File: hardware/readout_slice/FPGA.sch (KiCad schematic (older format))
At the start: 0 parts

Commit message: more work on moving FPGA components around
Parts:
- added U? (x5): XC7A35T-1FGG484, symbol readout:XC7A35T-1FGG484
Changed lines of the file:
@@
 $Descr A4 11693 8268
 encoding utf-8
-Sheet 1 4
+Sheet 4 4
 Title ""
 Date ""
@@
 Comment4 ""
 $EndDescr
+$Comp
+L readout:XC7A35T-1FGG484 U?
+U 4 1 6056B4FB
+P 1900 4550
+AR Path="/6056B4FB" Ref="U?"  Part="4"
+AR Path="/605605C8/6056B4FB" Ref="U?"  Part="4"
+F 0 "U?" H 1950 777 50  0000 C CNN
+F 1 "XC7A35T-1FGG484" H 1950 686 50  0000 C CNN
+F 2 "" H 800 4700 50  0001 C CNN
+F 3 "" H 800 4700 50  0001 C CNN
+	4    1900 4550
+	1    0    0    -1
+$EndComp
+$Comp
+L readout:XC7A35T-1FGG484 U?
+U 5 1 6056B501
+P 2150 -450
+AR Path="/6056B501" Ref="U?"  Part="5"
+AR Path="/605605C8/6056B501" Ref="U?"  Part="5"
+F 0 "U?" H 1825 -4223 50  0000 C CNN
+F 1 "XC7A35T-1FGG484" H 1825 -4314 50  0000 C CNN
+F 2 "" H 1050 -300 50  0001 C CNN
+F 3 "" H 1050 -300 50  0001 C CNN
+	5    2150 -450
+	1    0    0    -1
+$EndComp
+$Comp
+L readout:XC7A35T-1FGG484 U?
+U 6 1 6056B507
+P 5250 -50
+AR Path="/6056B507" Ref="U?"  Part="6"
+AR Path="/605605C8/6056B507" Ref="U?"  Part="6"
+F 0 "U?" H 5125 -3823 50  0000 C CNN
+F 1 "XC7A35T-1FGG484" H 5125 -3914 50  0000 C CNN
+F 2 "" H 4150 100 50  0001 C CNN
+F 3 "" H 4150 100 50  0001 C CNN
+	6    5250 -50
+	1    0    0    -1
+$EndComp
+$Comp
+L readout:XC7A35T-1FGG484 U?
+U 7 1 6057AABA
+P 8250 1800
+F 0 "U?" H 8125 -1973 50  0000 C CNN
+F 1 "XC7A35T-1FGG484" H 8125 -2064 50  0000 C CNN
+F 2 "" H 7150 1950 50  0001 C CNN
+F 3 "" H 7150 1950 50  0001 C CNN
+	7    8250 1800
+	1    0    0    -1
+$EndComp
+$Comp
+L readout:XC7A35T-1FGG484 U?
+U 8 1 6057AAC0
+P 11600 1550
+F 0 "U?" H 11225 -2223 50  0000 C CNN
+F 1 "XC7A35T-1FGG484" H 11225 -2314 50  0000 C CNN
+F 2 "" H 10500 1700 50  0001 C CNN
+F 3 "" H 10500 1700 50  0001 C CNN
+	8    11600 1550
+	1    0    0    -1
+$EndComp
 $EndSCHEMATC

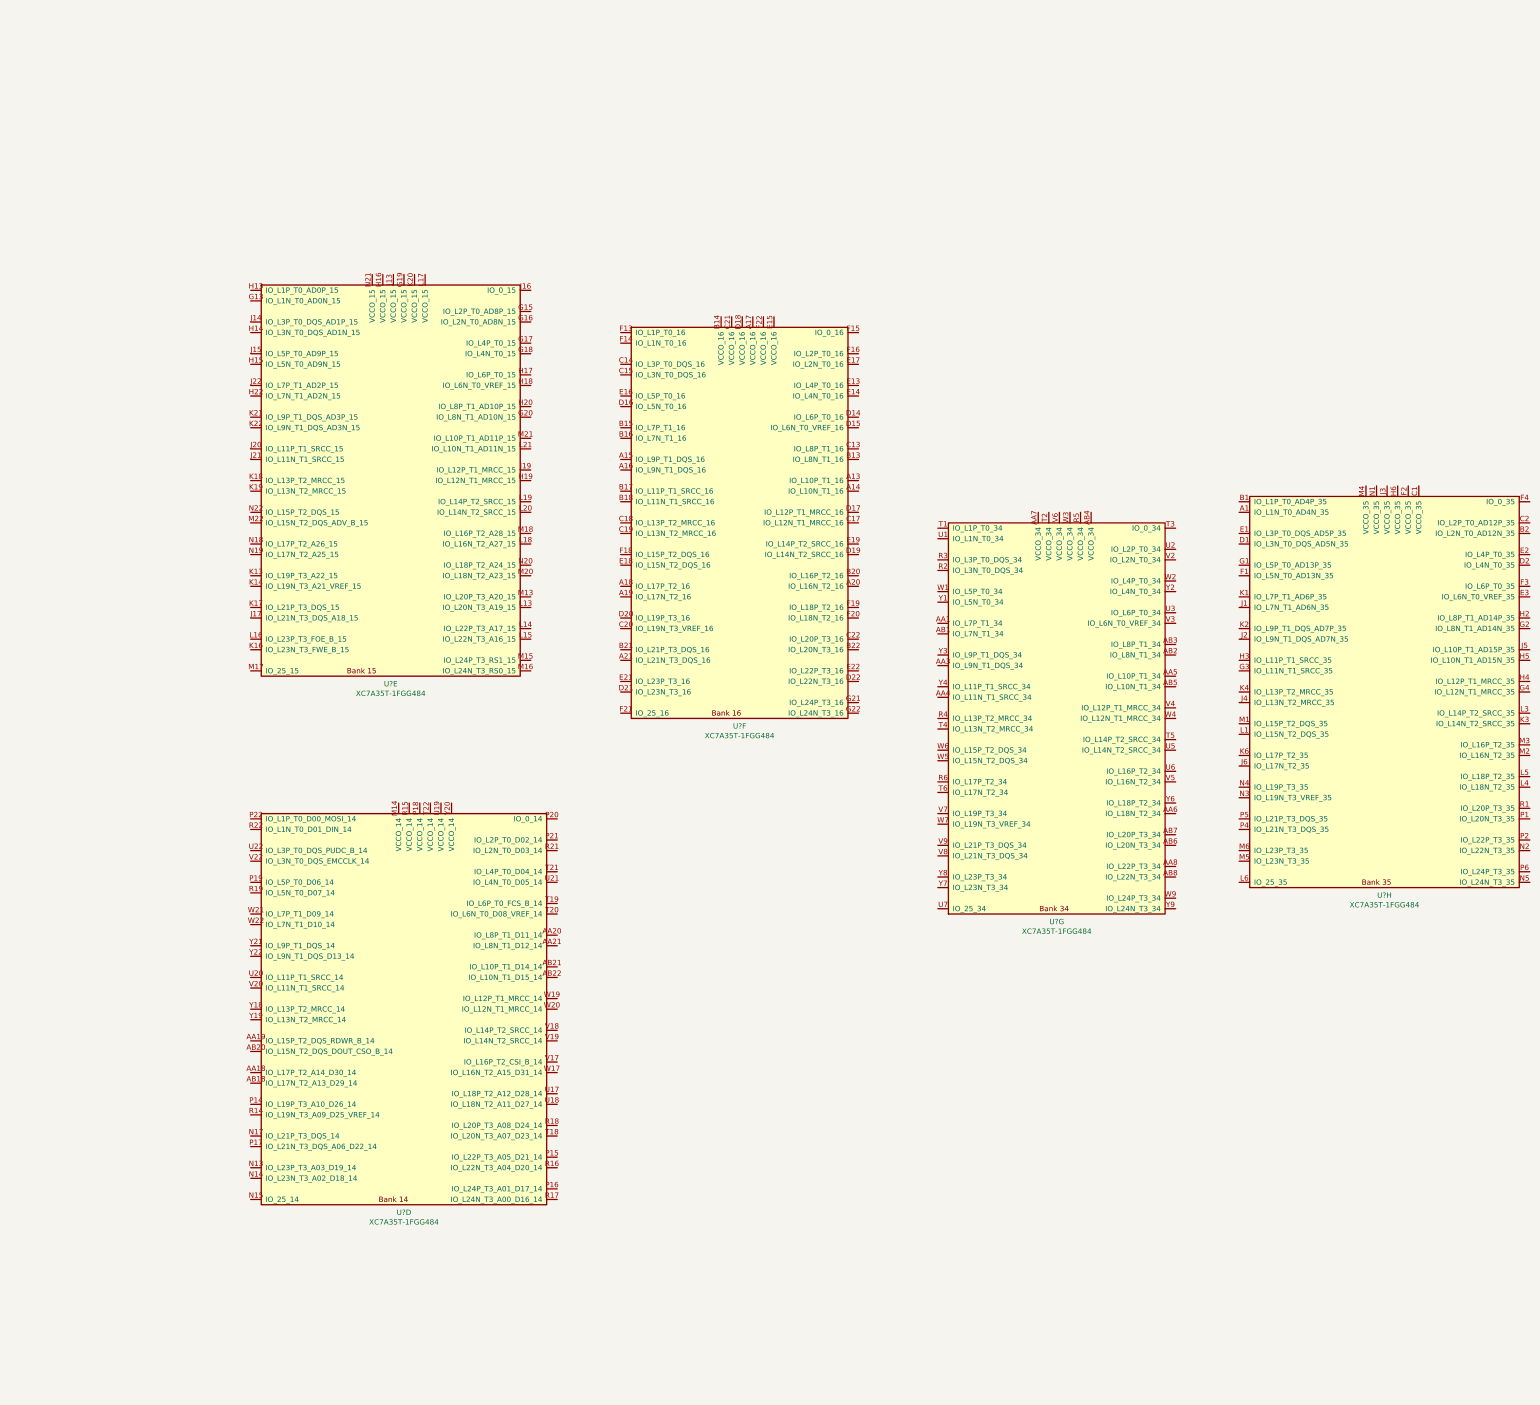
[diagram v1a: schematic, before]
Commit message: more work on readout connectivity
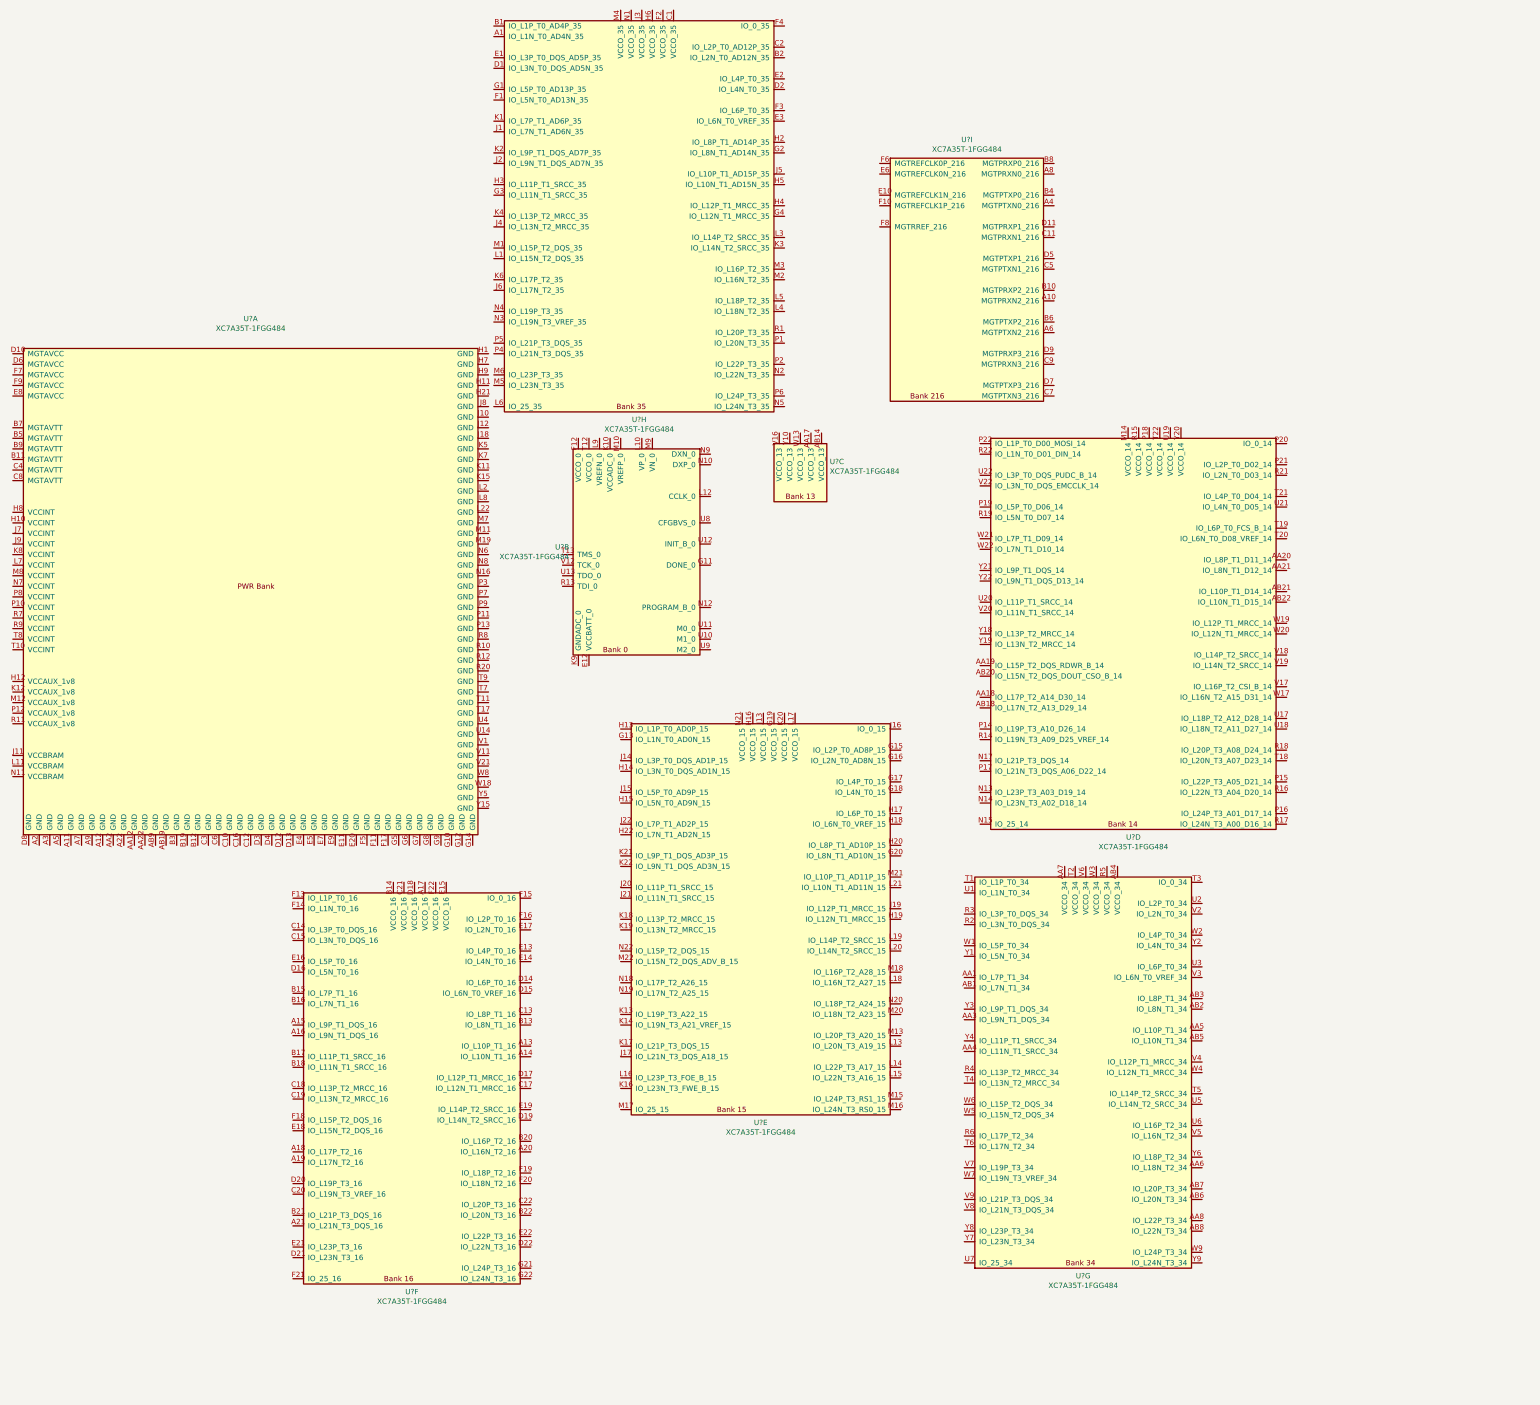
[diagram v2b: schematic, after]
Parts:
- removed U? (x5): XC7A35T-1FGG484, symbol readout:XC7A35T-1FGG484
- added U? (x9): XC7A35T-1FGG484, symbol readout:XC7A35T-1FGG484
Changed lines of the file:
@@
 $Comp
 L readout:XC7A35T-1FGG484 U?
-U 4 1 6056B4FB
-P 1900 4550
-AR Path="/6056B4FB" Ref="U?"  Part="4"
-AR Path="/605605C8/6056B4FB" Ref="U?"  Part="4"
-F 0 "U?" H 1950 777 50  0000 C CNN
-F 1 "XC7A35T-1FGG484" H 1950 686 50  0000 C CNN
-F 2 "" H 800 4700 50  0001 C CNN
-F 3 "" H 800 4700 50  0001 C CNN
-	4    1900 4550
+U 1 1 604A9F40
+P 650 150
+F 0 "U?" H 500 431 50  0000 C CNN
+F 1 "XC7A35T-1FGG484" H 500 340 50  0000 C CNN
+F 2 "" H -450 300 50  0001 C CNN
+F 3 "" H -450 300 50  0001 C CNN
+	1    650  150
 	1    0    0    -1
 $EndComp
 $Comp
 L readout:XC7A35T-1FGG484 U?
-U 5 1 6056B501
-P 2150 -450
-AR Path="/6056B501" Ref="U?"  Part="5"
-AR Path="/605605C8/6056B501" Ref="U?"  Part="5"
-F 0 "U?" H 1825 -4223 50  0000 C CNN
-F 1 "XC7A35T-1FGG484" H 1825 -4314 50  0000 C CNN
-F 2 "" H 1050 -300 50  0001 C CNN
-F 3 "" H 1050 -300 50  0001 C CNN
-	5    2150 -450
+U 2 1 604B4183
+P 4350 1100
+F 0 "U?" H 3513 171 50  0000 R CNN
+F 1 "XC7A35T-1FGG484" H 3513 80  50  0000 R CNN
+F 2 "" H 3250 1250 50  0001 C CNN
+F 3 "" H 3250 1250 50  0001 C CNN
+	2    4350 1100
 	1    0    0    -1
 $EndComp
 $Comp
 L readout:XC7A35T-1FGG484 U?
-U 6 1 6056B507
-P 5250 -50
-AR Path="/6056B507" Ref="U?"  Part="6"
-AR Path="/605605C8/6056B507" Ref="U?"  Part="6"
-F 0 "U?" H 5125 -3823 50  0000 C CNN
-F 1 "XC7A35T-1FGG484" H 5125 -3914 50  0000 C CNN
-F 2 "" H 4150 100 50  0001 C CNN
-F 3 "" H 4150 100 50  0001 C CNN
-	6    5250 -50
+U 3 1 604BC08F
+P 5700 1050
+F 0 "U?" H 5978 879 50  0000 L CNN
+F 1 "XC7A35T-1FGG484" H 5978 788 50  0000 L CNN
+F 2 "" H 4600 1200 50  0001 C CNN
+F 3 "" H 4600 1200 50  0001 C CNN
+	3    5700 1050
 	1    0    0    -1
 $EndComp
 $Comp
 L readout:XC7A35T-1FGG484 U?
-U 7 1 6057AABA
-P 8250 1800
-F 0 "U?" H 8125 -1973 50  0000 C CNN
-F 1 "XC7A35T-1FGG484" H 8125 -2064 50  0000 C CNN
-F 2 "" H 7150 1950 50  0001 C CNN
-F 3 "" H 7150 1950 50  0001 C CNN
-	7    8250 1800
+U 4 1 604C5353
+P 8800 1000
+F 0 "U?" H 8850 -2773 50  0000 C CNN
+F 1 "XC7A35T-1FGG484" H 8850 -2864 50  0000 C CNN
+F 2 "" H 7700 1150 50  0001 C CNN
+F 3 "" H 7700 1150 50  0001 C CNN
+	4    8800 1000
 	1    0    0    -1
 $EndComp
 $Comp
 L readout:XC7A35T-1FGG484 U?
-U 8 1 6057AAC0
-P 11600 1550
-F 0 "U?" H 11225 -2223 50  0000 C CNN
-F 1 "XC7A35T-1FGG484" H 11225 -2314 50  0000 C CNN
-F 2 "" H 10500 1700 50  0001 C CNN
-F 3 "" H 10500 1700 50  0001 C CNN
-	8    11600 1550
+U 5 1 604CE9F8
+P 5650 3700
+F 0 "U?" H 5325 -73 50  0000 C CNN
+F 1 "XC7A35T-1FGG484" H 5325 -164 50  0000 C CNN
+F 2 "" H 4550 3850 50  0001 C CNN
+F 3 "" H 4550 3850 50  0001 C CNN
+	5    5650 3700
 	1    0    0    -1
 $EndComp
+$Comp
+L readout:XC7A35T-1FGG484 U?
+U 6 1 604D9845
+P 2150 5300
+F 0 "U?" H 2025 1527 50  0000 C CNN
+F 1 "XC7A35T-1FGG484" H 2025 1436 50  0000 C CNN
+F 2 "" H 1050 5450 50  0001 C CNN
+F 3 "" H 1050 5450 50  0001 C CNN
+	6    2150 5300
+	1    0    0    -1
+$EndComp
+$Comp
+L readout:XC7A35T-1FGG484 U?
+U 7 1 604E2EDB
+P 8500 5150
+F 0 "U?" H 8375 1377 50  0000 C CNN
+F 1 "XC7A35T-1FGG484" H 8375 1286 50  0000 C CNN
+F 2 "" H 7400 5300 50  0001 C CNN
+F 3 "" H 7400 5300 50  0001 C CNN
+	7    8500 5150
+	1    0    0    -1
+$EndComp
+$Comp
+L readout:XC7A35T-1FGG484 U?
+U 8 1 604EB97A
+P 4550 -2950
+F 0 "U?" H 4175 -6723 50  0000 C CNN
+F 1 "XC7A35T-1FGG484" H 4175 -6814 50  0000 C CNN
+F 2 "" H 3450 -2800 50  0001 C CNN
+F 3 "" H 3450 -2800 50  0001 C CNN
+	8    4550 -2950
+	1    0    0    -1
+$EndComp
+$Comp
+L readout:XC7A35T-1FGG484 U?
+U 9 1 6050DA52
+P 7350 -1650
+F 0 "U?" H 7275 -1475 50  0000 C CNN
+F 1 "XC7A35T-1FGG484" H 7275 -1566 50  0000 C CNN
+F 2 "" H 6250 -1500 50  0001 C CNN
+F 3 "" H 6250 -1500 50  0001 C CNN
+	9    7350 -1650
+	1    0    0    -1
+$EndComp

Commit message: more work on readout_slice
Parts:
- removed U?: XC7A35T-1FGG484, symbol readout:XC7A35T-1FGG484
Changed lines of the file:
@@
-$Comp
-L readout:XC7A35T-1FGG484 U?
-U 1 1 604A9F40
-P 650 150
-F 0 "U?" H 500 431 50  0000 C CNN
-F 1 "XC7A35T-1FGG484" H 500 340 50  0000 C CNN
-F 2 "" H -450 300 50  0001 C CNN
-F 3 "" H -450 300 50  0001 C CNN
-	1    650  150
-	1    0    0    -1
-$EndComp
 $Comp
 L readout:XC7A35T-1FGG484 U?

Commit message: working more on readout_slice schematic
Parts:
- removed U?: XC7A35T-1FGG484, symbol readout:XC7A35T-1FGG484
- added C? (x6): 47u, symbol Device:C_Small
- added C? (x12): 4.7u, symbol Device:C_Small
- added C? (x24): .47u, symbol Device:C_Small
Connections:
- net Vcc_0: now reaches U?.M14 (VCCO_14)
- net Vcc_0: now also U?.P18 (VCCO_14), U?.R15 (VCCO_14), U?.T22 (VCCO_14), U?.U19 (VCCO_14), U?.Y20 (VCCO_14), C?.1, C?.1, C?.1, C?.1, C?.1, C?.1, C?.1
- net at U?.C1 (VCCO_35): now also U?.F2 (VCCO_35), U?.H6 (VCCO_35), U?.J3 (VCCO_35), U?.M4 (VCCO_35), U?.N1 (VCCO_35), C?.1, C?.1, C?.1, C?.1, C?.1, C?.1, C?.1
- new net GNDD: C?.2, C?.2, C?.2, C?.2, C?.2, C?.2, C?.2, C?.2, C?.2, C?.2, C?.2, C?.2, C?.2, C?.2
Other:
- moved on the sheet: U?C, U?D, U?E, U?F, U?G, U?H, U?I

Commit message: auto push run at Mon Mar 15 12:11:48 EDT 2021
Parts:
- removed C? (x2): 47u, symbol Device:C_Small
- removed C? (x4): 4.7u, symbol Device:C_Small
- removed C? (x8): .47u, symbol Device:C_Small
- removed U? (x2): XC7A35T-1FGG484, symbol readout:XC7A35T-1FGG484
